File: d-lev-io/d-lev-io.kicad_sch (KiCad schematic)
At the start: 11 parts, among them J1 PJ-059A, J2 USB_C_Receptacle_USB2.0, J8 Conn_01x12_MountingPin, U1 AMS1117-5.0

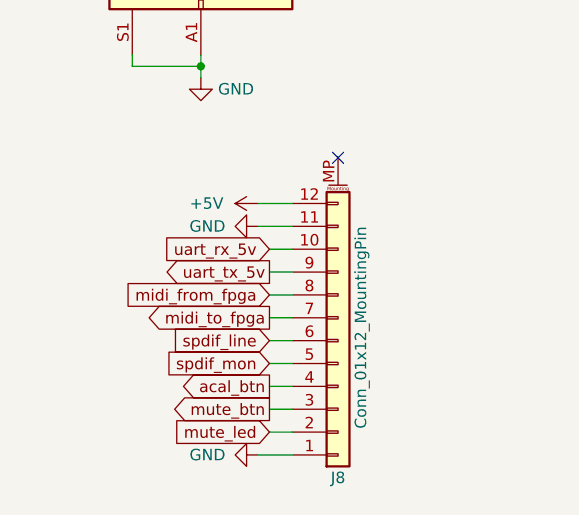
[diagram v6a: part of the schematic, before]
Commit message: Pinned out FPGA and rearranged encoders again
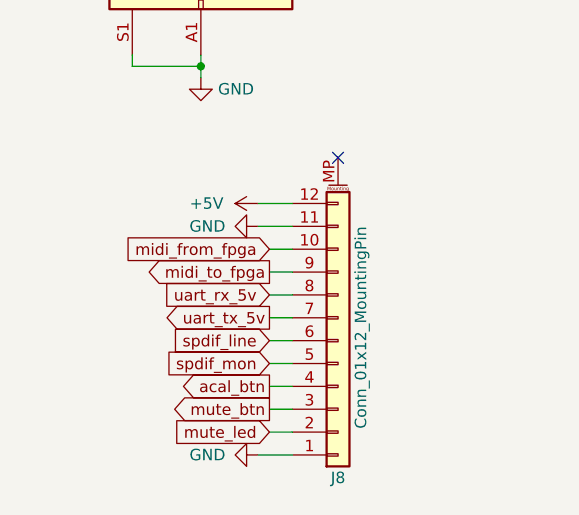
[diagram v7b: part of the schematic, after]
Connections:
- net midi_from_fpga: now also J8.10 (Pin_10); no longer J8.8 (Pin_8)
- net midi_to_fpga: now also J8.9 (Pin_9); no longer J8.7 (Pin_7)
- net uart_rx_5v: now also J8.8 (Pin_8); no longer J8.10 (Pin_10)
- net uart_tx_5v: now also J8.7 (Pin_7); no longer J8.9 (Pin_9)
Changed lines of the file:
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@@
     )
   )
-  (global_label "midi_to_fpga" (shape output) (at 34.29 123.19 180) (fields_autoplaced)
+  (global_label "midi_to_fpga" (shape output) (at 34.29 118.11 180) (fields_autoplaced)
     (effects (font (size 1.27 1.27)) (justify right))
     (property "Intersheetrefs" "${INTERSHEET_REFS}" (at 19.3497 123.19 0)
@@
     )
   )
-  (global_label "uart_tx_5v" (shape output) (at 34.29 118.11 180) (fields_autoplaced)
+  (global_label "uart_tx_5v" (shape output) (at 34.29 123.19 180) (fields_autoplaced)
     (effects (font (size 1.27 1.27)) (justify right))
     (property "Intersheetrefs" "${INTERSHEET_REFS}" (at 21.7082 118.11 0)
@@
     )
   )
-  (global_label "uart_rx_5v" (shape input) (at 34.29 115.57 180) (fields_autoplaced)
+  (global_label "uart_rx_5v" (shape input) (at 34.29 120.65 180) (fields_autoplaced)
     (effects (font (size 1.27 1.27)) (justify right))
     (property "Intersheetrefs" "${INTERSHEET_REFS}" (at 21.6477 115.57 0)
@@
     )
   )
-  (global_label "midi_from_fpga" (shape input) (at 34.29 120.65 180) (fields_autoplaced)
+  (global_label "midi_from_fpga" (shape input) (at 34.29 115.57 180) (fields_autoplaced)
     (effects (font (size 1.27 1.27)) (justify right))
     (property "Intersheetrefs" "${INTERSHEET_REFS}" (at 16.8702 120.65 0)

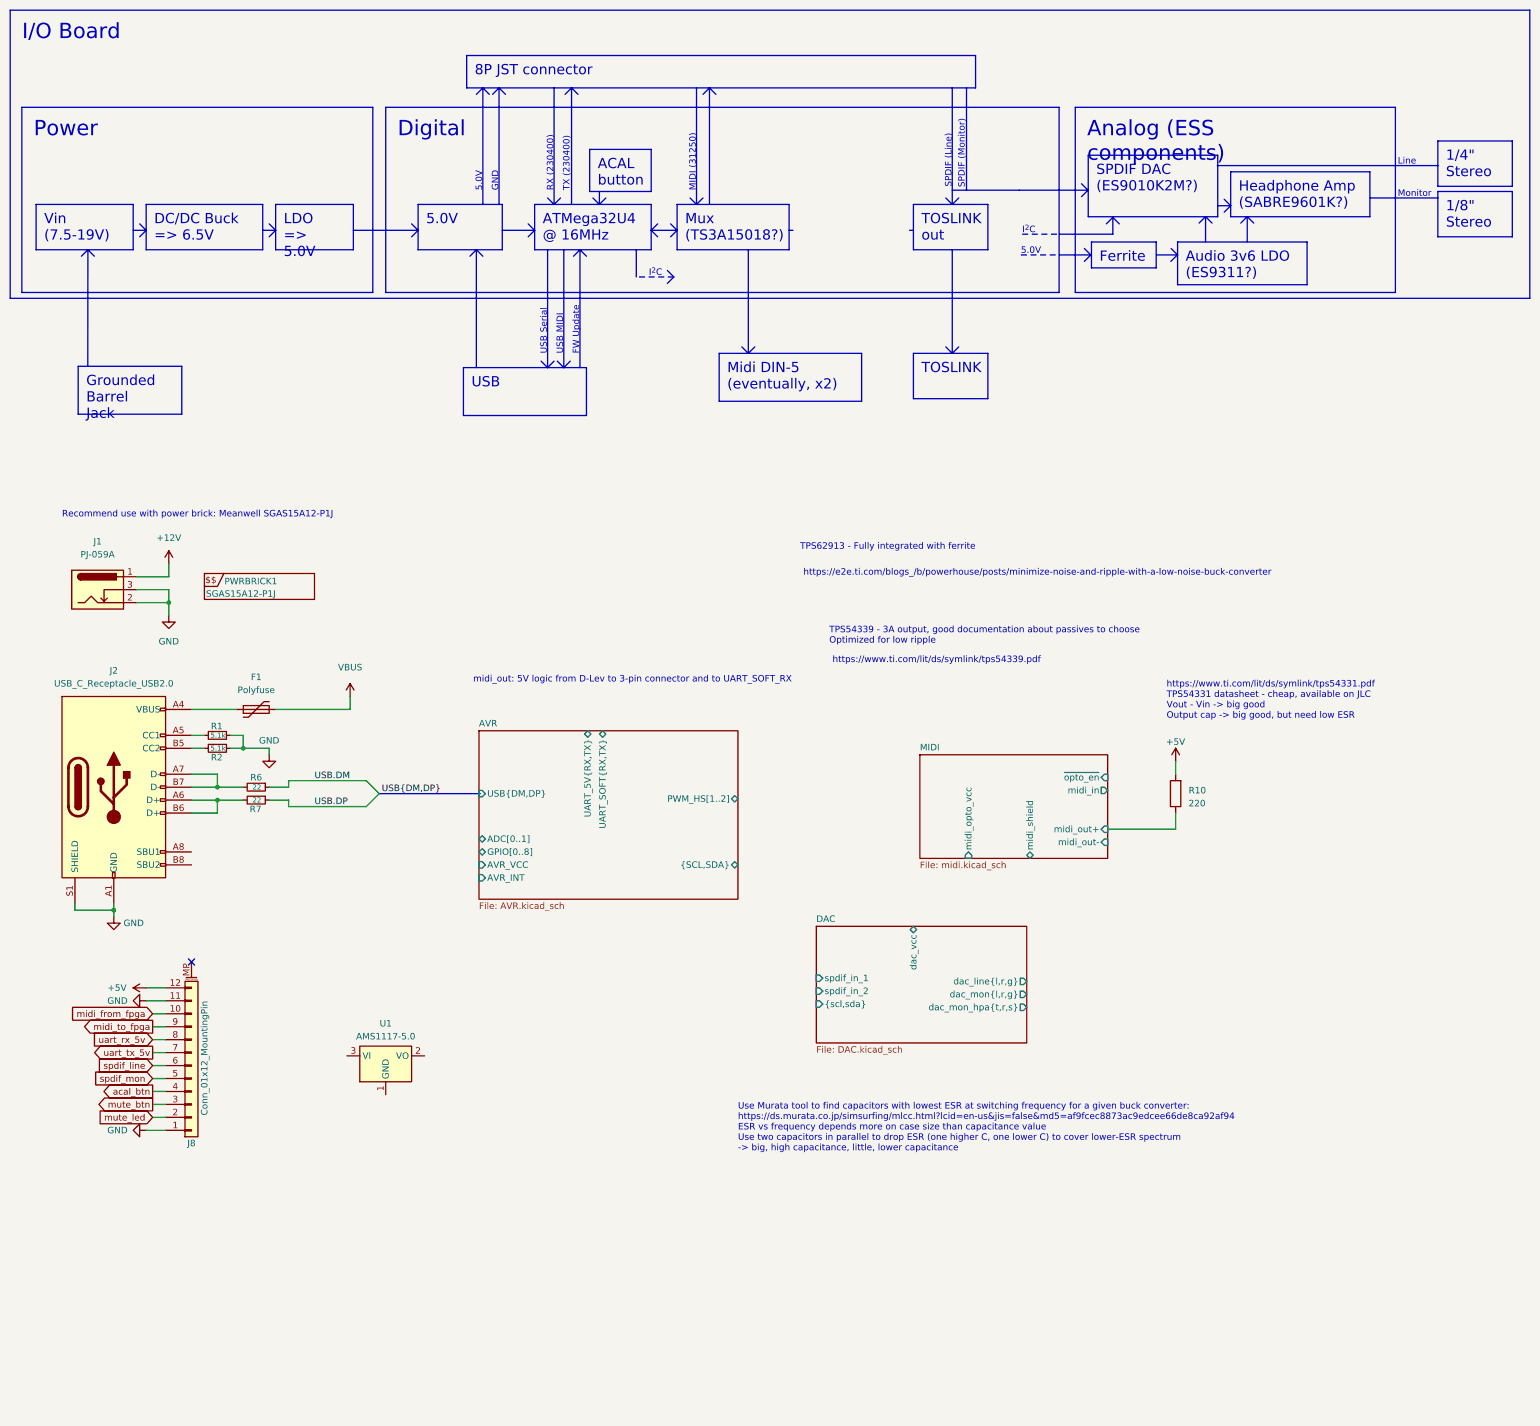
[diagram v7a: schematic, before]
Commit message: Built out power circuitry on d-lev-io
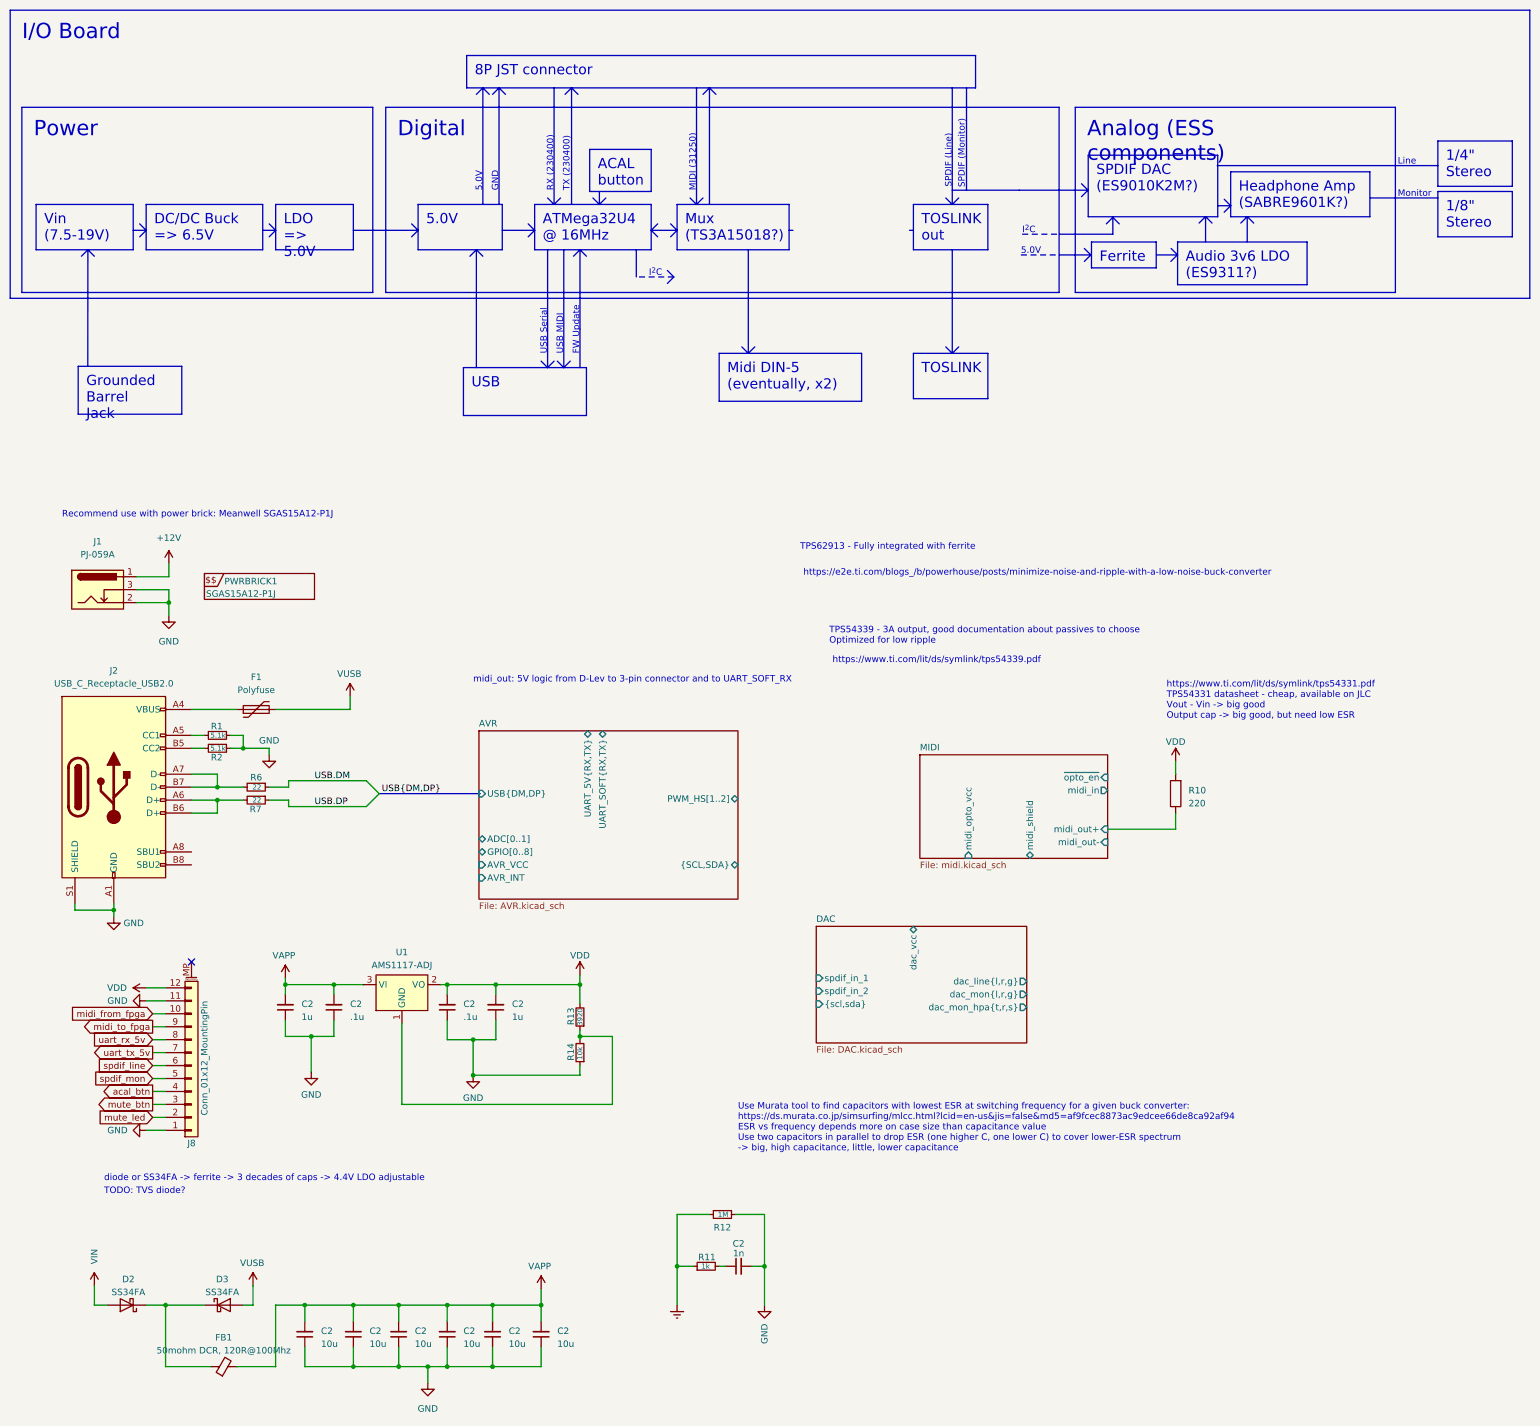
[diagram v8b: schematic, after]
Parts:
- added C2 (x6): 10u, symbol Device:C_Small
- added C2 (x2): .1u, symbol Device:C_Small
- added C2 (x2): 1u, symbol Device:C_Small
- added C2: 1n, symbol Device:C_Small
- added D2, D3: SS34FA, symbol Device:D_Schottky
- added FB1: 50mohm DCR, 120R@100Mhz, Inductor_SMD:L_0201_0603Metric, symbol Device:FerriteBead_Small
- added R11: 1k, Resistor_SMD:R_0805_2012Metric_Pad1.20x1.40mm_HandSolder, symbol Device:R_Small
- added R12: 1M, Resistor_SMD:R_0805_2012Metric_Pad1.20x1.40mm_HandSolder, symbol Device:R_Small
- added R13: 3920, Resistor_SMD:R_0805_2012Metric_Pad1.20x1.40mm_HandSolder, symbol Device:R_Small
- added R14: 10k, Resistor_SMD:R_0805_2012Metric_Pad1.20x1.40mm_HandSolder, symbol Device:R_Small
- U1: value AMS1117-5.0 -> AMS1117-ADJ
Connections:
- net +5V: now also U1.2 (VO), C2.2, C2.2, D2.2 (A), R13.2
- net GND: now also C2.1, C2.1, C2.1, C2.1, C2.1, C2.1, C2.1, C2.1, C2.1, C2.1, C2.2, R12.1, R14.1
- net VBUS: now also U1.3 (VI), C2.2, C2.2, C2.2, C2.2, C2.2, C2.2, C2.2, C2.2, D3.2 (A), FB1.2
- net at U1.1 (GND): now also R13.1, R14.2
- new net: C2.1, R11.2
- new net: D2.1 (K), D3.1 (K), FB1.1
- new net Earth: R11.1, R12.2
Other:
- note added: "TODO: TVS diode?"
- note added: "diode or SS34FA -> ferrite -> 3 decades of caps -> 4.4V LDO adjustable"
- moved on the sheet: U1
